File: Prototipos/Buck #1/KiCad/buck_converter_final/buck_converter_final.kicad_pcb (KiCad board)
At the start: 2 copper layers, 50 x 100 mm, 39 parts, among them J2 Screw_Terminal_01x02, J3 Screw_Terminal_01x02, K1 SANYOU_SRD_Form_C, Q1 NPN, Q2 IRF9540NPBF, Q3 BC548

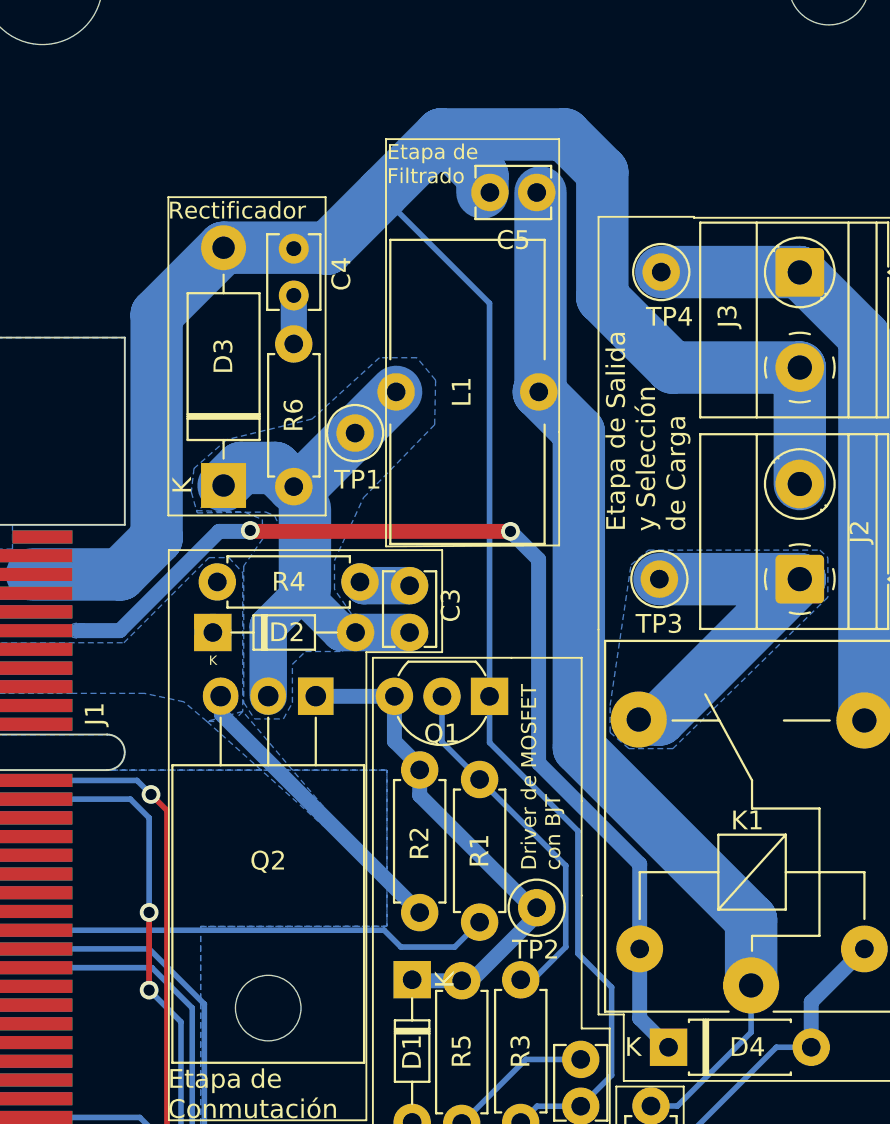
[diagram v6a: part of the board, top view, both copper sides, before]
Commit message: Corrección footprint diodo
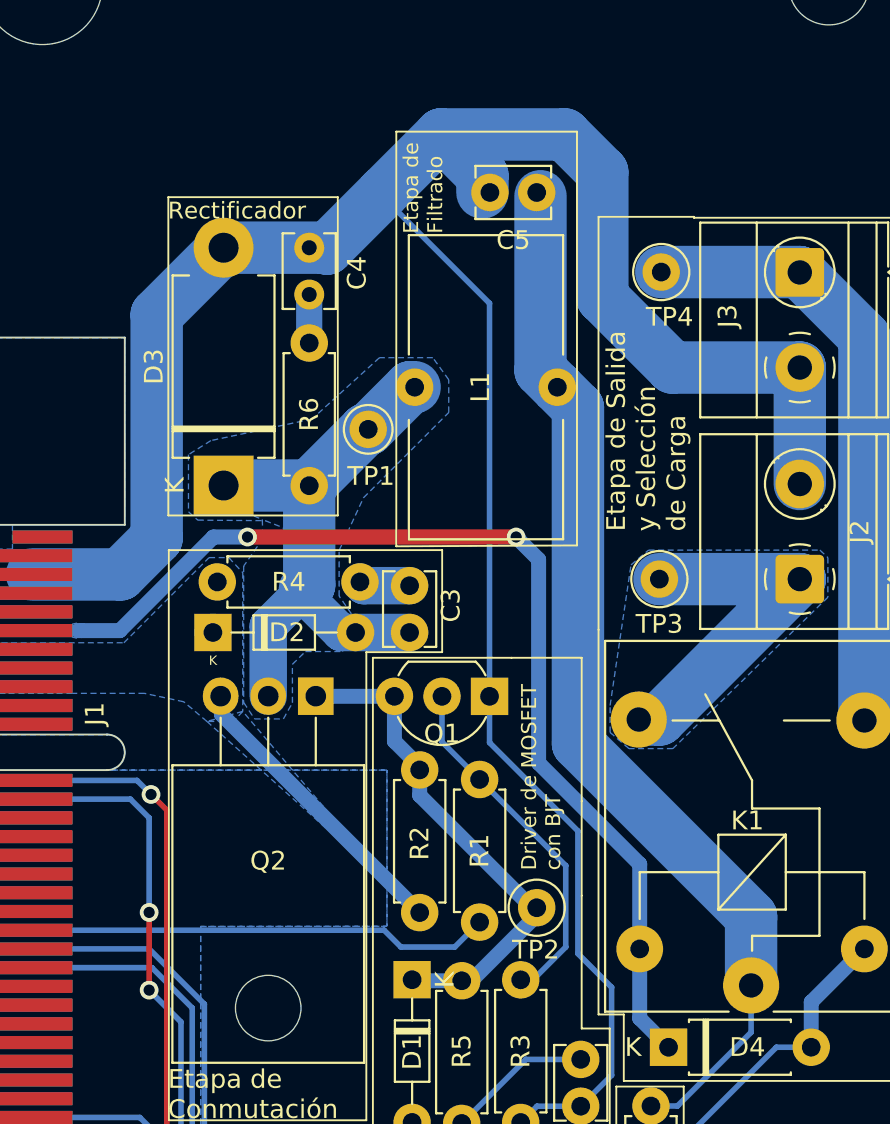
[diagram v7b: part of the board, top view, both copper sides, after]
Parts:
- D3: footprint Diode_THT:D_DO-15_P12.70mm_Horizontal -> Diode_THT:D_DO-201AD_P12.70mm_Horizontal
- moved L1 1.02 mm to (128.7, 58.5)
- moved C4 0.83 mm to (123.0, 53.5)
- moved R6 0.83 mm to (123.0, 63.8)
- moved TP1 0.73 mm to (126.2, 60.8)
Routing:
- net Net-(D2-A): track 29.7 -> 31.3 mm

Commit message: Avances en medición de corriente
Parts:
- added C7: 0.1uF, Capacitor_SMD:C_0805_2012Metric_Pad1.18x1.45mm_HandSolder, B.Cu at (142.1, 61.6)
- added R14: 0.01, Resistor_SMD:R_0805_2012Metric_Pad1.20x1.40mm_HandSolder, B.Cu at (136.3, 61.9)
- added TP5: INDUCOR_CURRENT, TestPoint:TestPoint_Loop_D1.80mm_Drill1.0mm_Beaded, F.Cu at (139.4, 58.5)
- added U1: INA199xxDCK, Package_TO_SOT_SMD:SOT-363_SC-70-6, B.Cu at (139.2, 62.0)
- R10: value 2k2 -> 2.2k
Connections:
- C5 pad 1: Net-(C5-Pad1) -> Net-(U1--)
- K1 pad 1: Net-(C5-Pad1) -> Net-(U1--)
- L1 pad 2: Net-(C5-Pad1) -> Net-(U1-+)
- R9 pad 1: Net-(C5-Pad1) -> Net-(U1--)
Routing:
- net Net-(U1--): track 0.00 -> 64.5 mm
- net Net-(C5-Pad1): track 56.3 -> 0.00 mm
- net 12V: track 16.0 -> 48.2 mm, vias 0 -> 2
- net PGND: track 167.2 -> 173.4 mm
- net Net-(U1-+): track 0.00 -> 5.02 mm
- net Net-(TP5-Pad1): track 0.00 -> 3.38 mm
- net 5Vdc: track 58.7 -> 57.4 mm
- removed copper zone on B.Cu, net 5Vdc
